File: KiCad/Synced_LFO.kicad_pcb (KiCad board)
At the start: 2 copper layers, 29.2 x 101.6 mm, 51 parts, among them J1 UP Out, J2 CLK In, J3 BP Inv, J4 BP Out, J5 Power, P1 B100K, P2 B100K, P3 B100K, P4 B100K, U1 TL072, U2 TL072

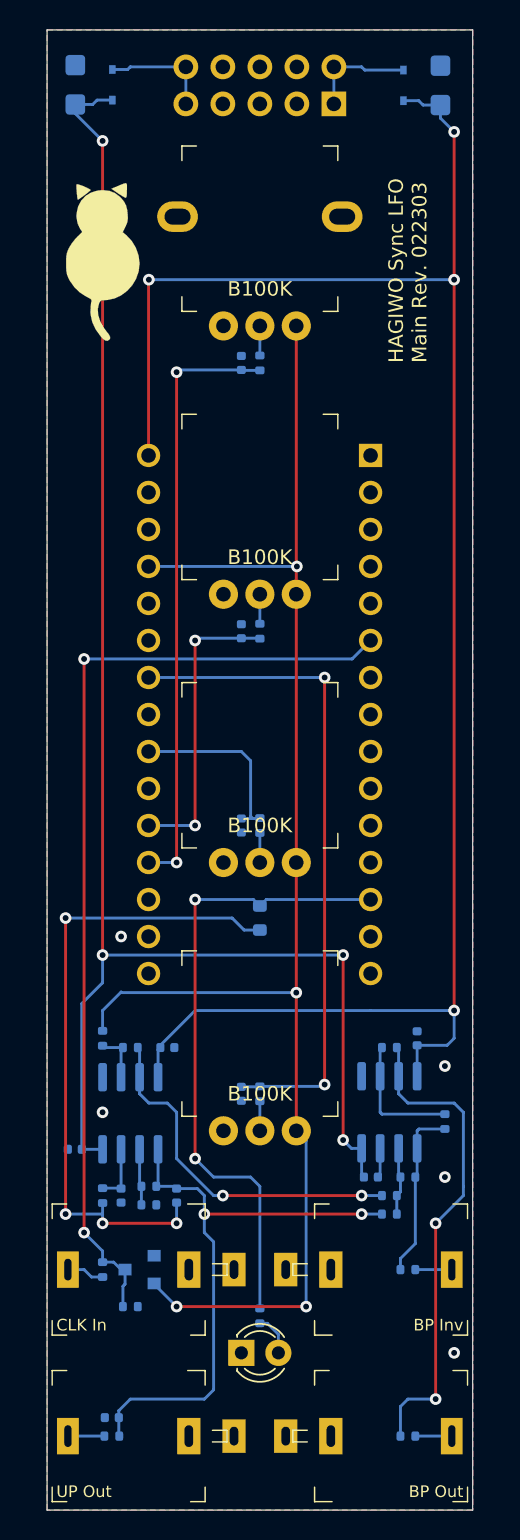
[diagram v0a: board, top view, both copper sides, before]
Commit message: fixing power in sch; placing components; connecting pads and coppering
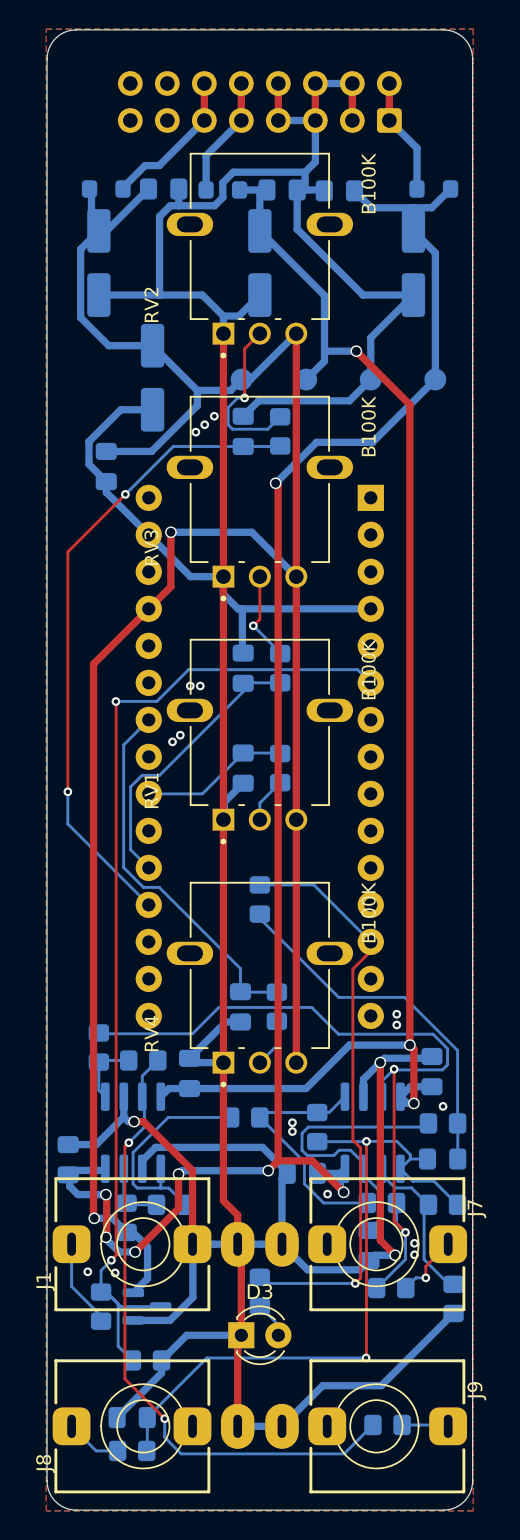
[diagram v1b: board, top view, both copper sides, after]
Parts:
- removed D2: LED, LED_THT:LED_D3.0mm
- removed D4: 1N5819, Diode_SMD:D_SOD-323
- removed G***: LOGO, CATs_Eurosynth_Specials:CATs Tiny
- removed J2: CLK In, Connector_Audio_QingPu:Jack_3.5mm_QingPu_WQP-PJ301M-12
- removed J3: BP Inv, Connector_Audio_QingPu:Jack_3.5mm_QingPu_WQP-PJ301M-12
- removed J4: BP Out, Connector_Audio_QingPu:Jack_3.5mm_QingPu_WQP-PJ301M-12
- removed P1, P3, P4: B100K, Potentiometer_THT_Additional:Potentiometer_AlpsAlpine_RK09L1140_wo_Fix
- removed P2: B100K, Potentiometer_THT_Additional:Potentiometer_AlpsAlpine_RK09L1140
- removed U1, U2: TL072, Package_SO:SOIC-8_3.9x4.9mm_P1.27mm
- added C14: 100nF, Capacitor_SMD:C_0805_2012Metric_Pad1.18x1.45mm_HandSolder, B.Cu at (20.1, 11.0)
- added C15: 10uF, Capacitor_SMD:CP_Elec_5x5.4, B.Cu at (3.56, 16.0)
- added C16: 10uF, Capacitor_SMD:CP_Elec_5x5.4, B.Cu at (14.6, 16.0)
- added C17: 10uF, Capacitor_SMD:CP_Elec_5x5.4, B.Cu at (25.1, 16.0)
- added C18: 100nF, Capacitor_SMD:C_0805_2012Metric_Pad1.18x1.45mm_HandSolder, B.Cu at (4.06, 30.0)
- added C19: 10uF, Capacitor_SMD:CP_Elec_5x5.4, B.Cu at (7.24, 23.9)
- added FB1: FerriteBead_Small, Inductor_SMD:L_0805_2012Metric_Pad1.05x1.20mm_HandSolder, B.Cu at (4.06, 10.9)
- added FB2: FerriteBead_Small, Inductor_SMD:L_0805_2012Metric_Pad1.05x1.20mm_HandSolder, B.Cu at (12.1, 11.0)
- added FB3: FerriteBead_Small, Inductor_SMD:L_0805_2012Metric_Pad1.05x1.20mm_HandSolder, B.Cu at (26.5, 10.9)
- added J7: BP_Inv_Out, Eurorack:Jack_3.5mm_QingPu_WQP-PJ398SM_Vertical, F.Cu at (22.6, 83.3)
- added J8: UP_Out, Eurorack:Jack_3.5mm_QingPu_WQP-PJ398SM_Vertical, F.Cu at (6.60, 95.8)
- added J9: BP_Out, Eurorack:Jack_3.5mm_QingPu_WQP-PJ398SM_Vertical, F.Cu at (22.6, 95.8)
- added RV1: B100K, Eurorack:Potentiometer_Alpha_RD901F_Vertical_Alt, F.Cu at (14.6, 46.7)
- added RV2: B100K, Eurorack:Potentiometer_Alpha_RD901F_Vertical_Alt, F.Cu at (14.6, 13.3)
- added RV3: B100K, Eurorack:Potentiometer_Alpha_RD901F_Vertical_Alt, F.Cu at (14.6, 30.0)
- added RV4: B100K, Eurorack:Potentiometer_Alpha_RD901F_Vertical_Alt, F.Cu at (14.6, 63.4)
- added TP1: +5V, TestPoint:TestPoint_Pad_D1.5mm, B.Cu at (13.3, 24.0)
- added TP2: +12V, TestPoint:TestPoint_Pad_D1.5mm, B.Cu at (17.8, 24.0)
- added TP3: GND, TestPoint:TestPoint_Pad_D1.5mm, B.Cu at (22.2, 24.0)
- added TP4: -12V, TestPoint:TestPoint_Pad_D1.5mm, B.Cu at (26.6, 24.0)
- added U3: TL072, Package_SO:SOIC-8_3.9x4.9mm_P1.27mm, B.Cu at (22.4, 75.7)
- added U4: TL072, Package_SO:SOIC-8_3.9x4.9mm_P1.27mm, B.Cu at (5.90, 75.7)
- A1: footprint Module:Arduino_Nano -> Eurorack:Arduino_Nano
- C1, C2: footprint Capacitor_SMD:C_0402_1005Metric -> Capacitor_SMD:C_0805_2012Metric_Pad1.18x1.45mm_HandSolder
- C10, C12, C13, C9: value 100n -> 100nF; footprint Capacitor_SMD:C_0402_1005Metric -> Capacitor_SMD:C_0805_2012Metric_Pad1.18x1.45mm_HandSolder
- C11, C8: value 10u -> 100nF; footprint Capacitor_Tantalum_SMD:CP_EIA-3216-18_Kemet-A -> Capacitor_SMD:C_0805_2012Metric_Pad1.18x1.45mm_HandSolder
- C3: value 220p -> 6.8n; footprint Capacitor_SMD:C_0402_1005Metric -> Capacitor_SMD:C_0805_2012Metric_Pad1.18x1.45mm_HandSolder
- C4: value 220p -> 10n; footprint Capacitor_SMD:C_0402_1005Metric -> Capacitor_SMD:C_0805_2012Metric_Pad1.18x1.45mm_HandSolder
- C5: value 6.8n -> 220p; footprint Capacitor_SMD:C_0402_1005Metric -> Capacitor_SMD:C_0805_2012Metric_Pad1.18x1.45mm_HandSolder
- C6: value 10n -> 100n; footprint Capacitor_SMD:C_0402_1005Metric -> Capacitor_SMD:C_0805_2012Metric_Pad1.18x1.45mm_HandSolder
- C7: value 100n -> 220p; footprint Capacitor_SMD:C_0402_1005Metric -> Capacitor_SMD:C_0805_2012Metric_Pad1.18x1.45mm_HandSolder
- D3: value 1N5819 -> LED; footprint Diode_SMD:D_SOD-323 -> LED_THT:LED_D3.0mm_Clear; moved to F.Cu
- J1: value UP Out -> CLK In; footprint Connector_Audio_QingPu:Jack_3.5mm_QingPu_WQP-PJ301M-12 -> Eurorack:Jack_3.5mm_QingPu_WQP-PJ398SM_Vertical
- J5: value Power -> Eurorack Connector; footprint CATs_Eurosynth_Specials:Power_2x5_Vertical -> Connector_IDC:IDC-Header_2x08_P2.54mm_Vertical
- R1: value 470R -> 1k; footprint Resistor_SMD:R_0402_1005Metric -> Resistor_SMD:R_0805_2012Metric_Pad1.20x1.40mm_HandSolder
- R10: value 1k -> 13k; footprint Resistor_SMD:R_0402_1005Metric -> Resistor_SMD:R_0805_2012Metric_Pad1.20x1.40mm_HandSolder
- R11: value 10k -> 27k; footprint Resistor_SMD:R_0402_1005Metric -> Resistor_SMD:R_0805_2012Metric_Pad1.20x1.40mm_HandSolder
- R12: value 100k -> 20k; footprint Resistor_SMD:R_0402_1005Metric -> Resistor_SMD:R_0805_2012Metric_Pad1.20x1.40mm_HandSolder
- R13: value 10k -> 470R; footprint Resistor_SMD:R_0402_1005Metric -> Resistor_SMD:R_0805_2012Metric_Pad1.20x1.40mm_HandSolder
- R14, R17, R18, R4, R9: footprint Resistor_SMD:R_0402_1005Metric -> Resistor_SMD:R_0805_2012Metric_Pad1.20x1.40mm_HandSolder
- R15, R19, R20: value 10k -> 1k; footprint Resistor_SMD:R_0402_1005Metric -> Resistor_SMD:R_0805_2012Metric_Pad1.20x1.40mm_HandSolder
- R16: value 1k -> 10k; footprint Resistor_SMD:R_0402_1005Metric -> Resistor_SMD:R_0805_2012Metric_Pad1.20x1.40mm_HandSolder
- R2: value 470R -> 100k; footprint Resistor_SMD:R_0402_1005Metric -> Resistor_SMD:R_0805_2012Metric_Pad1.20x1.40mm_HandSolder
- R21: value 1k -> 470R; footprint Resistor_SMD:R_0402_1005Metric -> Resistor_SMD:R_0805_2012Metric_Pad1.20x1.40mm_HandSolder
- R3: value 470R -> 10k; footprint Resistor_SMD:R_0402_1005Metric -> Resistor_SMD:R_0805_2012Metric_Pad1.20x1.40mm_HandSolder
- R5: value 13k -> 10k; footprint Resistor_SMD:R_0603_1608Metric -> Resistor_SMD:R_0805_2012Metric_Pad1.20x1.40mm_HandSolder
- R6: value 27k -> 470R; footprint Resistor_SMD:R_0402_1005Metric -> Resistor_SMD:R_0805_2012Metric_Pad1.20x1.40mm_HandSolder
- R7: value 1k -> 300R; footprint Resistor_SMD:R_0402_1005Metric -> Resistor_SMD:R_0805_2012Metric_Pad1.20x1.40mm_HandSolder
- R8: value 300R -> 10k; footprint Resistor_SMD:R_0402_1005Metric -> Resistor_SMD:R_0805_2012Metric_Pad1.20x1.40mm_HandSolder
- moved D3 86.5 mm to (13.3, 89.6), turned to 0 degrees
- moved C11 73.8 mm to (1.45, 77.5)
- moved R2 68.9 mm to (6.86, 91.3), turned to 180 degrees
- moved C13 68.0 mm to (16.1, 11.0)
- moved C8 67.7 mm to (26.4, 71.5)
- moved C12 66.2 mm to (8.00, 10.9), turned to 0 degrees
- moved R6 53.8 mm to (16.0, 27.6), turned to 90 degrees
- moved R3 41.3 mm to (5.46, 81.5), turned to -90 degrees
- moved C3 38.8 mm to (27.1, 77.5), turned to 0 degrees
- moved R13 38.2 mm to (16.0, 43.8), turned to 90 degrees
- moved C5 36.5 mm to (13.5, 43.8), turned to 90 degrees
- moved R1 34.8 mm to (3.71, 87.6)
- moved R19 32.8 mm to (5.84, 97.5), turned to 0 degrees
- moved R21 30.8 mm to (15.8, 67.0), turned to -90 degrees
- moved C7 29.5 mm to (13.3, 67.1), turned to -90 degrees
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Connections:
- A1 pad 1: (no net) -> unconnected-(A1-D1/TX-Pad1)
- A1 pad 10: (no net) -> unconnected-(A1-D7-Pad10)
- A1 pad 11: (no net) -> unconnected-(A1-D8-Pad11)
- A1 pad 12: (no net) -> unconnected-(A1-D9-Pad12)
- A1 pad 13: D10 -> PWM OUT
- A1 pad 14: (no net) -> unconnected-(A1-D11-Pad14)
- A1 pad 15: (no net) -> unconnected-(A1-D12-Pad15)
- A1 pad 16: (no net) -> unconnected-(A1-D13-Pad16)
- A1 pad 17: (no net) -> unconnected-(A1-3V3-Pad17)
- A1 pad 18: (no net) -> unconnected-(A1-AREF-Pad18)
- A1 pad 19: A0 -> AMP
- A1 pad 2: (no net) -> unconnected-(A1-D0/RX-Pad2)
- A1 pad 20: A1 -> PHASE
- A1 pad 21: (no net) -> unconnected-(A1-A2-Pad21)
- A1 pad 22: A3 -> WAVEFORM
- A1 pad 23: (no net) -> unconnected-(A1-A4-Pad23)
- A1 pad 24: A5 -> MODULATION
- A1 pad 25: (no net) -> unconnected-(A1-A6-Pad25)
- A1 pad 26: (no net) -> unconnected-(A1-A7-Pad26)
- A1 pad 28: (no net) -> unconnected-(A1-~{RESET}-Pad28)
- A1 pad 3: (no net) -> unconnected-(A1-~{RESET}-Pad3)
- A1 pad 30: +12V -> unconnected-(A1-VIN-Pad30)
- A1 pad 5: (no net) -> unconnected-(A1-D2-Pad5)
- A1 pad 6: D3 -> CLOCK
- A1 pad 7: (no net) -> unconnected-(A1-D4-Pad7)
- A1 pad 8: (no net) -> unconnected-(A1-D5-Pad8)
- A1 pad 9: (no net) -> unconnected-(A1-D6-Pad9)
- C1 pad 1: A3 -> WAVEFORM
- C10 pad 1: GND -> +12V
- C10 pad 2: +12V -> GND
- C12 pad 1: -12V -> +5V
- C13 pad 1: -12V -> +12V
- C2 pad 1: A0 -> AMP
- C3 pad 1: A1 -> Out
- C3 pad 2: GND -> Net-(C3-Pad2)
- C4 pad 1: A5 -> GND
- C4 pad 2: GND -> Net-(U3A-+)
- C5 pad 1: Out -> PHASE
- C5 pad 2: Net-(C5-Pad2) -> GND
- C6 pad 2: Net-(C6-Pad2) -> Out
- C7 pad 1: GND -> MODULATION
- C7 pad 2: Out -> GND
- C9 pad 2: +12V -> -12V
- D1 pad 3: D3 -> CLOCK
- D3 pad 1: +12V -> GND
- D3 pad 2: Net-(D3-Pad2) -> Net-(D3-A)
- J1 pad TN: (no net) -> GND
- R1 pad 1: A3 -> CLOCK
- R1 pad 2: Net-(P1-PadW) -> Net-(J1-PadT)
- R10 pad 1: D3 -> Net-(C3-Pad2)
- R10 pad 2: Net-(J2-PadT) -> PWM OUT
- R11 pad 1: GND -> Net-(U3A-+)
- R11 pad 2: Net-(R11-Pad2) -> Net-(C3-Pad2)
- R12 pad 1: GND -> Net-(R12-Pad1)
- R12 pad 2: D3 -> Net-(U3B-+)
- R13 pad 1: Net-(R13-Pad1) -> PHASE
- R13 pad 2: Out -> Net-(R13-Pad2)
- R14 pad 1: Net-(R14-Pad1) -> GND
- R14 pad 2: Net-(R13-Pad1) -> Net-(U3A--)
- R15 pad 1: Net-(R13-Pad1) -> Net-(J7-PadT)
- R15 pad 2: -5VA -> Net-(R12-Pad1)
- R16 pad 1: Net-(J3-PadT) -> Net-(U4B-+)
- R16 pad 2: Net-(R14-Pad1) -> Net-(R12-Pad1)
- R17 pad 1: -5VA -> Out
- R17 pad 2: Net-(R17-Pad2) -> Net-(U3A--)
- R18 pad 1: Net-(R17-Pad2) -> Net-(R18-Pad1)
- R18 pad 2: +5V -> Net-(U4B-+)
- R19 pad 1: Net-(R19-Pad1) -> Net-(J8-PadT)
- R19 pad 2: Net-(R19-Pad2) -> Out
- R2 pad 1: A0 -> GND
- R2 pad 2: Net-(P2-PadW) -> CLOCK
- R20 pad 1: Net-(R19-Pad2) -> Net-(J9-PadT)
- R20 pad 2: Net-(R14-Pad1) -> Net-(R18-Pad1)
- R21 pad 1: Net-(J4-PadT) -> MODULATION
- R21 pad 2: Net-(R19-Pad1) -> Net-(R21-Pad2)
- R3 pad 1: A1 -> Net-(U4A-+)
- R3 pad 2: Net-(P3-PadW) -> +5V
- R4 pad 1: A5 -> WAVEFORM
- R5 pad 1: Net-(C5-Pad2) -> -5V
- R5 pad 2: D10 -> Net-(U4A-+)
- R6 pad 1: Net-(C6-Pad2) -> AMP
- R6 pad 2: Net-(C5-Pad2) -> Net-(R6-Pad2)
- R7 pad 1: Net-(J1-PadT) -> Net-(D3-A)
- R7 pad 2: Out -> PWM OUT
- R8 pad 1: Net-(D2-Pad2) -> Net-(U3B-+)
- R8 pad 2: D10 -> Out
- R9 pad 1: Out -> Net-(U3B-+)
- R9 pad 2: Net-(R11-Pad2) -> -5V
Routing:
- net GND: track 2.03 -> 308.4 mm, vias 5 -> 20
- net CLOCK: track 0.00 -> 69.8 mm, vias 0 -> 2
- net D3: track 66.5 -> 0.00 mm, vias 2 -> 0
- net +5V: track 104.1 -> 158.2 mm, vias 4 -> 2
- net Net-(R12-Pad1): track 0.00 -> 51.5 mm, vias 0 -> 2
- net A5: track 45.8 -> 0.00 mm, vias 2 -> 0
- net Net-(C5-Pad2): track 44.4 -> 0.00 mm, vias 4 -> 0
- net AMP: track 0.00 -> 44.1 mm, vias 0 -> 2
- net D10: track 43.8 -> 0.00 mm, vias 2 -> 0
- net Net-(R18-Pad1): track 0.00 -> 43.6 mm, vias 0 -> 2
- net A0: track 41.4 -> 0.00 mm, vias 2 -> 0
- net PWM OUT: track 0.00 -> 40.3 mm, vias 0 -> 1
- net +12V: track 128.4 -> 94.8 mm, vias 4 -> 3
- net Net-(R19-Pad1): track 33.3 -> 0.00 mm, vias 2 -> 0
- net MODULATION: track 0.00 -> 25.8 mm
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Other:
- outline, holes or cut-outs redrawn
- board text removed: "HAGIWO Sync LFO Main Rev. 022303"

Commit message: adding Logos on the pcb board
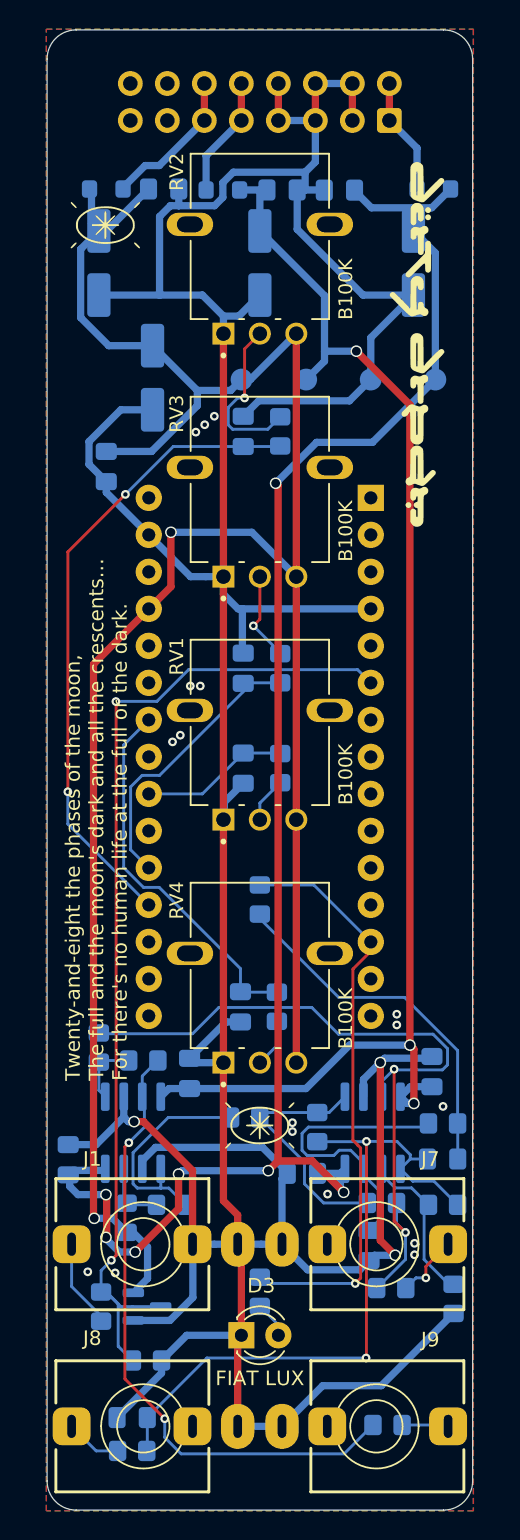
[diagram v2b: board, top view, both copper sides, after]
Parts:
- added G***: LOGO, LOGO, F.Cu at (25.4, 21.6)
- added G***: LOGO, LOGO, F.Cu at (4.48, 13.4)
- added G***: LOGO, LOGO, F.Cu at (14.1, 75.2)
- added G***: LOGO, LOGO, B.Cu at (14.8, 99.5)
- added G***: LOGO, LOGO, B.Cu at (25.9, 49.0)
- added G***: LOGO, LOGO, B.Cu at (2.73, 63.5)
- D3: value LED -> FIAT LUX
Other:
- board text added: "Chronophase LFO"
- board text added: "Designed in South Tyrol"
- board text added: "LOCKED TO TIME FREE IN FORM"
- board text added: "REV 1.0"
- board text added: "Twenty-and-eight the phases of the moon, The full and the moon's dark and all the crescents… For there's no human life at the full or the dark."
- board text added: "© Nathanael Noir 2026"
- board text added: "⇤"
- board text added: "⇱"

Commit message: generating gerber files
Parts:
- added G***: LOGO, LOGO, B.Cu at (2.72, 63.3)
- moved G*** 6.86 mm to (2.73, 56.6)
- moved R7 1.49 mm to (16.1, 86.7), turned to 0 degrees
- moved C10 0.24 mm to (9.54, 71.6)
- moved C16 0.07 mm to (14.6, 15.9)
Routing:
- net PWM OUT: track 40.3 -> 37.9 mm
- net +5V: track 158.2 -> 159.8 mm
- net Net-(D3-A): track 2.51 -> 3.23 mm
- net GND: track 308.4 -> 308.1 mm, vias 20 -> 19
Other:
- board text added: "30032026"
- board text added: "ID:"
